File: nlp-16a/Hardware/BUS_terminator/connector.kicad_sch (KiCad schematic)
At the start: 37 parts, among them J1 Conn_02x20_Odd_Even, J2 Conn_02x20_Odd_Even, J3 Conn_02x20_Odd_Even, J4 Conn_02x10_Odd_Even, J5 Screw_Terminal_01x02, J6 Conn_02x16_Odd_Even, J7 Conn_02x16_Odd_Even

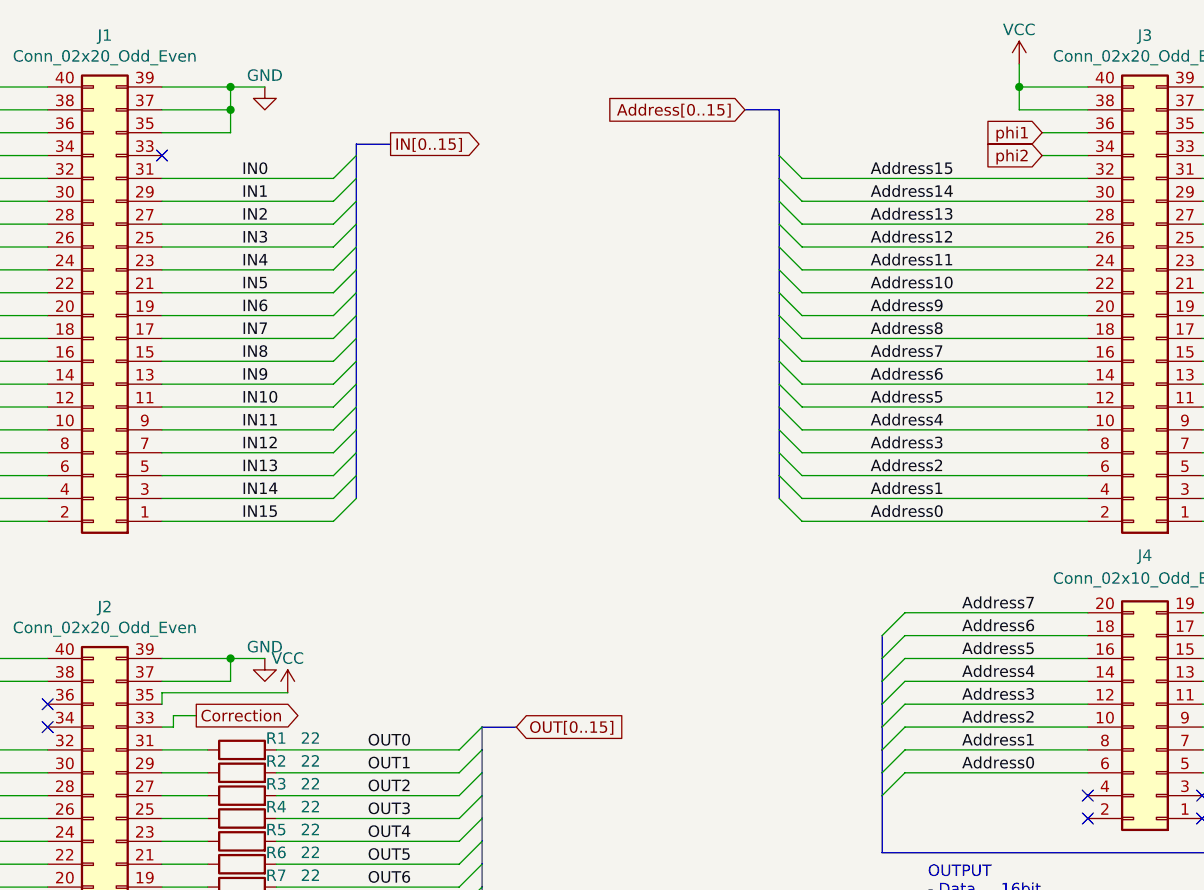
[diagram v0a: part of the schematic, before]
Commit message: バスターミネータのDMA機能は不要と判断したので削除．必要ならば外部回路で実現するように
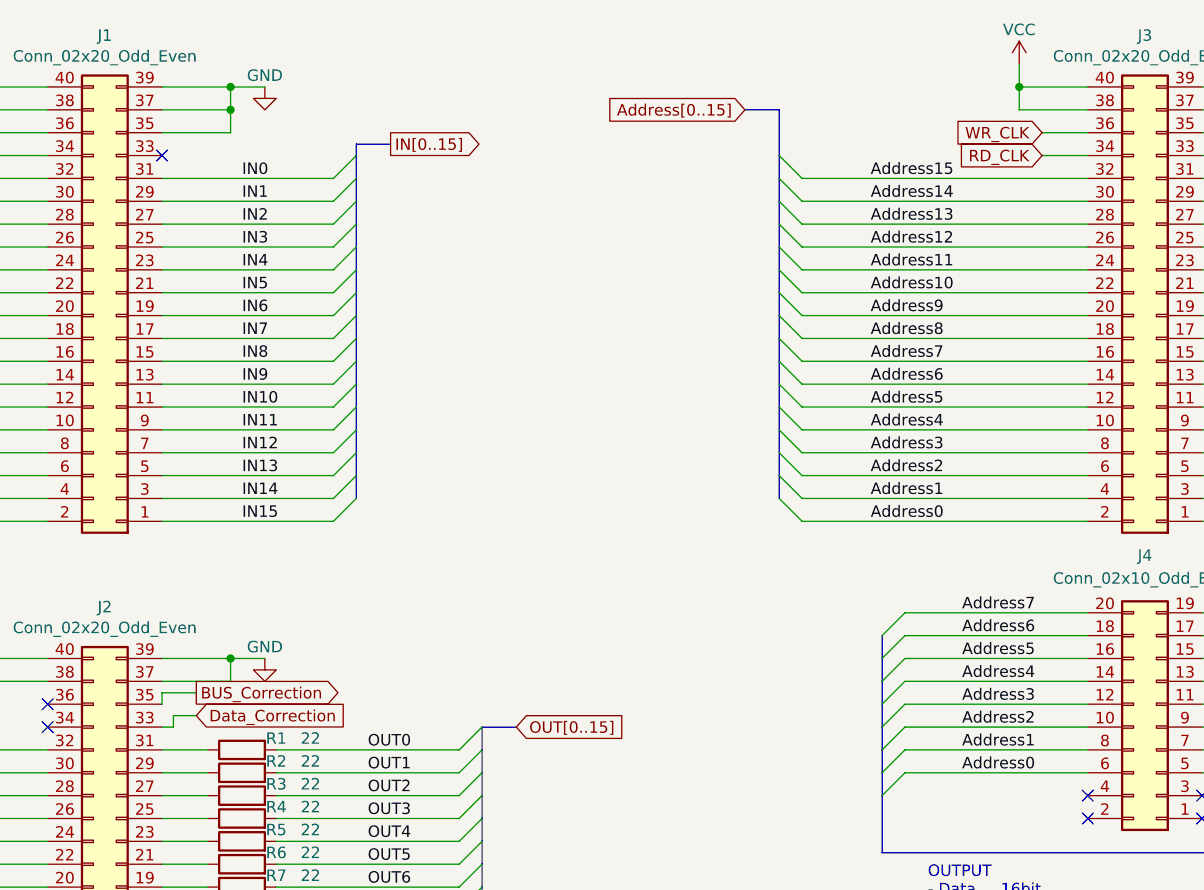
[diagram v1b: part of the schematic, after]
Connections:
- net VCC: no longer J2.35 (Pin_35)
- net phi1: no longer J3.36 (Pin_36)
- net phi2: no longer J3.34 (Pin_34)
- net Correction renamed Data_Correction
- new net BUS_Correction: J2.35 (Pin_35)
- new net RD_CLK: J3.34 (Pin_34)
- new net WR_CLK: J3.36 (Pin_36)
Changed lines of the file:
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@@
+    (stroke (width 0) (type default) (color 0 0 0 0))
+  )
+  (wire (pts (xy 101.6 87.63) (xy 105.41 87.63))
     (stroke (width 0) (type default) (color 0 0 0 0))
   )
@@
   )
   (wire (pts (xy 204.47 22.86) (xy 196.85 22.86))
-    (stroke (width 0) (type default) (color 0 0 0 0))
-  )
-  (wire (pts (xy 101.6 87.63) (xy 115.57 87.63))
     (stroke (width 0) (type default) (color 0 0 0 0))
   )
@@
     (effects (font (size 1.27 1.27)) (justify left bottom))
   )
-  (global_label "phi1" (shape input) (at 199.39 25.4 180) (fields_autoplaced)
+  (global_label "WR_CLK" (shape input) (at 199.39 25.4 180) (fields_autoplaced)
     (effects (font (size 1.27 1.27)) (justify right))
-    (property "Intersheet References" "${INTERSHEET_REFS}" (id 0) (at 192.8645 25.3206 0)
+    (property "Intersheet References" "${INTERSHEET_REFS}" (id 0) (at 189.7198 25.3206 0)
       (effects (font (size 1.27 1.27)) (justify right) hide)
     )
@@
     )
   )
-  (global_label "Correction" (shape output) (at 105.41 90.17 0) (fields_autoplaced)
+  (global_label "Data_Correction" (shape input) (at 105.41 90.17 0) (fields_autoplaced)
     (effects (font (size 1.27 1.27)) (justify left))
-    (property "Intersheet References" "${INTERSHEET_REFS}" (id 0) (at 117.6202 90.0906 0)
+    (property "Intersheet References" "${INTERSHEET_REFS}" (id 0) (at 122.8817 90.0906 0)
       (effects (font (size 1.27 1.27)) (justify left) hide)
     )
@@
     )
   )
+  (global_label "BUS_Correction" (shape output) (at 105.41 87.63 0) (fields_autoplaced)
+    (effects (font (size 1.27 1.27)) (justify left))
+    (property "Intersheet References" "${INTERSHEET_REFS}" (id 0) (at 122.3979 87.5506 0)
+      (effects (font (size 1.27 1.27)) (justify left) hide)
+    )
+  )
   (global_label "A_SEL" (shape output) (at 48.26 132.08 180) (fields_autoplaced)
     (effects (font (size 1.27 1.27)) (justify right))
@@
     )
   )
-  (global_label "phi2" (shape input) (at 199.39 27.94 180) (fields_autoplaced)
+  (global_label "RD_CLK" (shape input) (at 199.39 27.94 180) (fields_autoplaced)
     (effects (font (size 1.27 1.27)) (justify right))
-    (property "Intersheet References" "${INTERSHEET_REFS}" (id 0) (at 192.8645 27.8606 0)
+    (property "Intersheet References" "${INTERSHEET_REFS}" (id 0) (at 189.9012 27.8606 0)
       (effects (font (size 1.27 1.27)) (justify right) hide)
     )
@@
     (pin "2")
   )
-  (symbol (lib_id "power:VCC") (at 115.57 87.63 0) (mirror y) (unit 1)
-    (in_bom yes) (on_board yes)
-    (property "Reference" "#PWR08" (id 0) (at 115.57 91.44 0)
-      (effects (font (size 1.27 1.27)) hide)
-    )
-    (property "Value" "VCC" (id 1) (at 115.57 83.82 0))
-    (property "Footprint" "" (id 2) (at 115.57 87.63 0)
-      (effects (font (size 1.27 1.27)) hide)
-    )
-    (property "Datasheet" "" (id 3) (at 115.57 87.63 0)
-      (effects (font (size 1.27 1.27)) hide)
-    )
-    (pin "1")
-  )
   (symbol (lib_id "Device:C") (at 105.41 175.26 0) (unit 1)

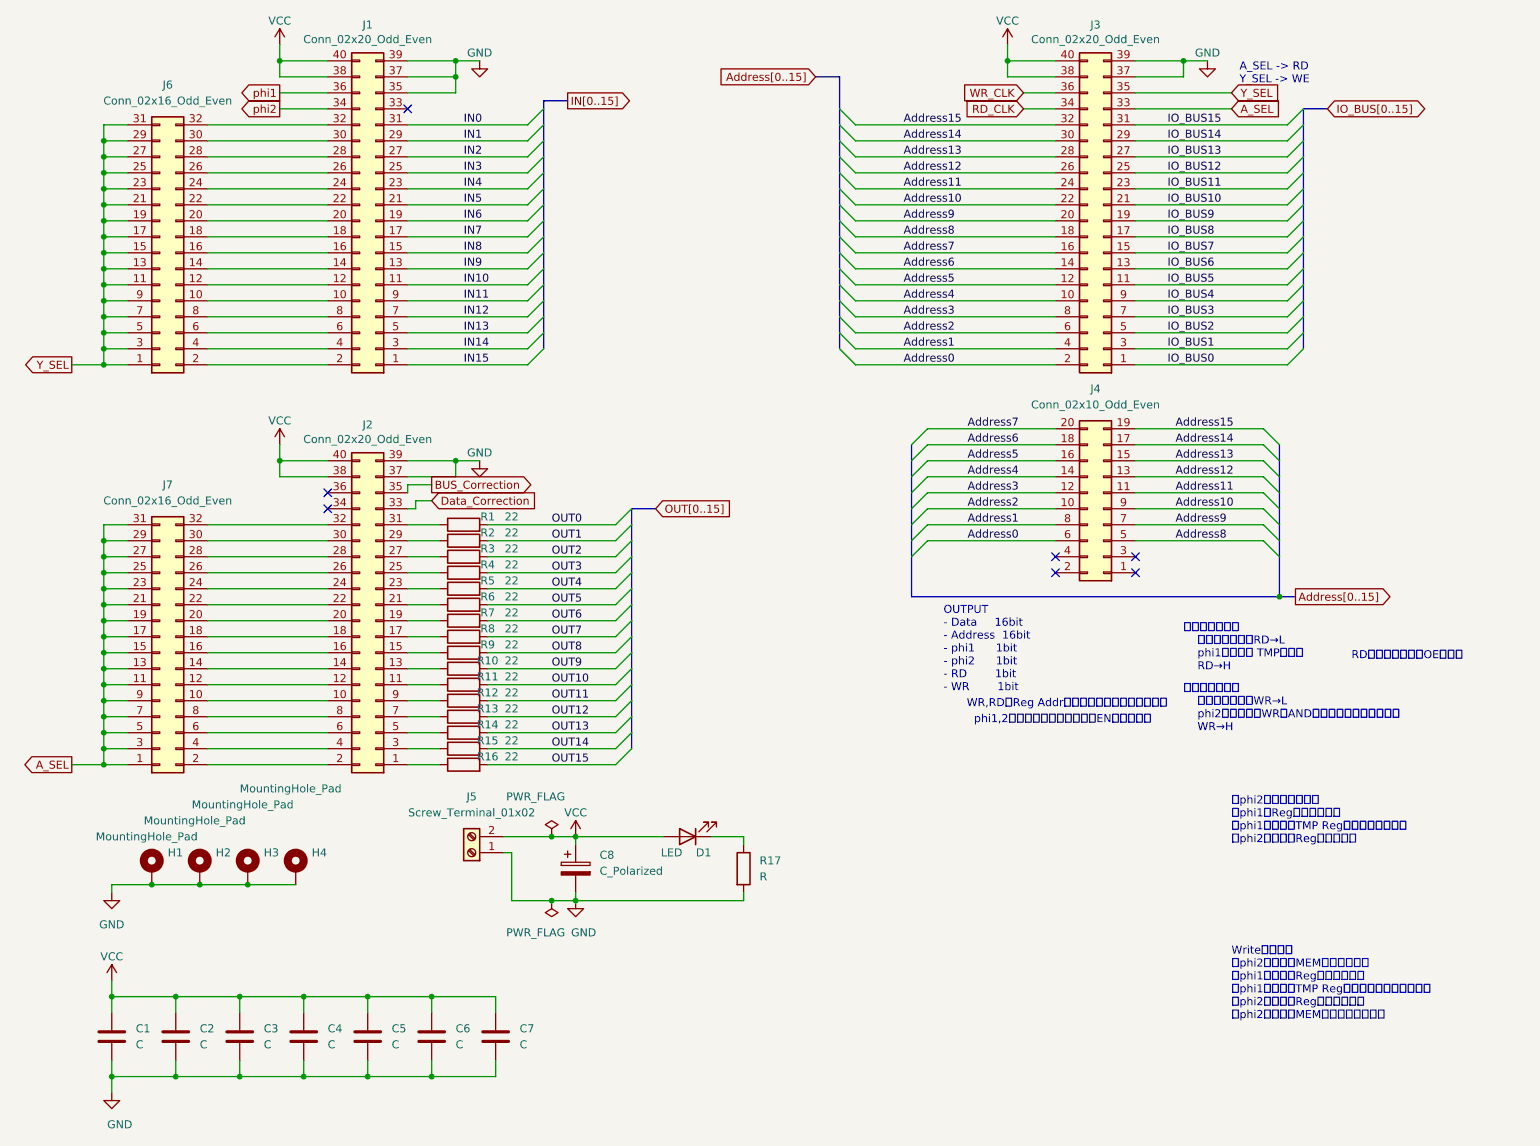
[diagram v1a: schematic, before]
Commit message: v1.1全ガーバーを更新
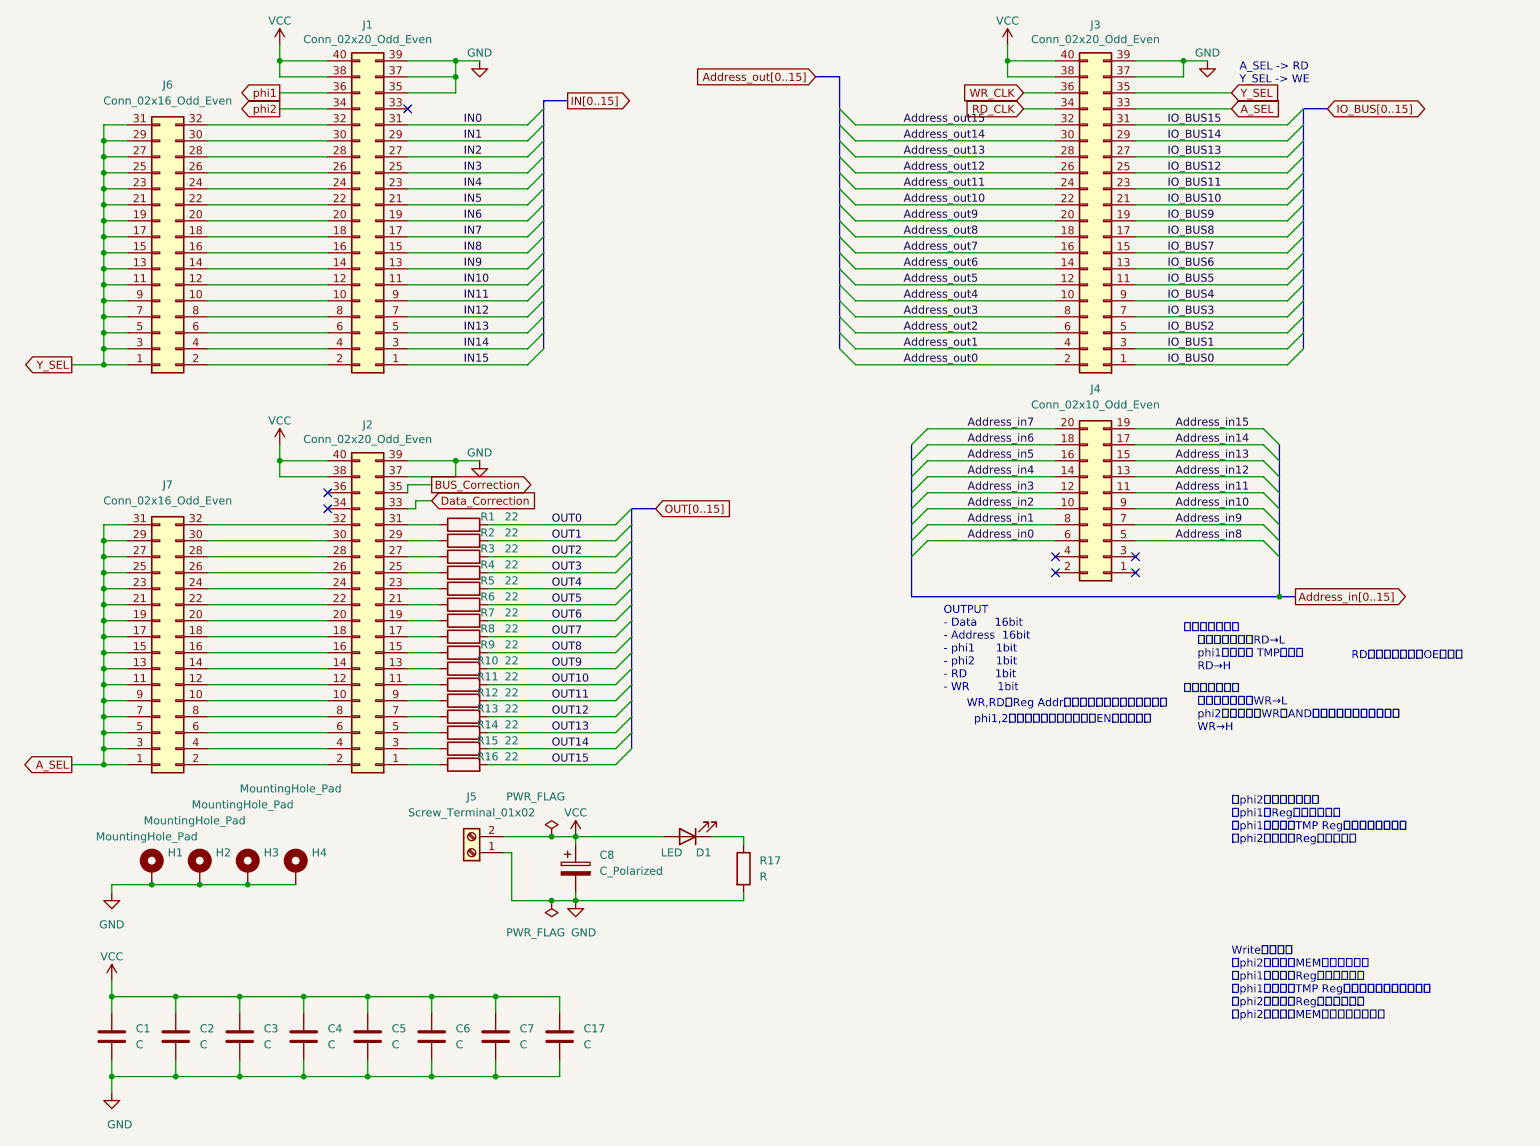
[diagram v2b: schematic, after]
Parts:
- added C17: C, Capacitor_THT:C_Disc_D7.0mm_W2.5mm_P5.00mm, symbol Device:C
- C1, C2, C3, C4, C5, C6, C7: footprint Capacitor_THT:C_Disc_D7.5mm_W2.5mm_P5.00mm -> Capacitor_THT:C_Disc_D7.0mm_W2.5mm_P5.00mm
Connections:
- net GND: now also C17.2
- net VCC: now also C17.1
- net Address0 renamed Address_in0
- net Address_in0: no longer J3.2 (Pin_2)
- net Address1 renamed Address_in1
- net Address_in1: no longer J3.4 (Pin_4)
- net Address10 renamed Address_in10
- net Address_in10: no longer J3.22 (Pin_22)
- net Address11 renamed Address_in11
- net Address_in11: no longer J3.24 (Pin_24)
- net Address12 renamed Address_in12
- net Address_in12: no longer J3.26 (Pin_26)
- net Address13 renamed Address_in13
- net Address_in13: no longer J3.28 (Pin_28)
- net Address14 renamed Address_in14
- net Address_in14: no longer J3.30 (Pin_30)
- net Address15 renamed Address_in15
- net Address_in15: no longer J3.32 (Pin_32)
- net Address2 renamed Address_in2
- net Address_in2: no longer J3.6 (Pin_6)
- net Address3 renamed Address_in3
- net Address_in3: no longer J3.8 (Pin_8)
- net Address4 renamed Address_in4
- net Address_in4: no longer J3.10 (Pin_10)
- net Address5 renamed Address_in5
- net Address_in5: no longer J3.12 (Pin_12)
- net Address6 renamed Address_in6
- net Address_in6: no longer J3.14 (Pin_14)
- net Address7 renamed Address_in7
- net Address_in7: no longer J3.16 (Pin_16)
- net Address8 renamed Address_in8
- net Address_in8: no longer J3.18 (Pin_18)
- net Address9 renamed Address_in9
- net Address_in9: no longer J3.20 (Pin_20)
- new net Address_out0: J3.2 (Pin_2)
- new net Address_out1: J3.4 (Pin_4)
- new net Address_out10: J3.22 (Pin_22)
- new net Address_out11: J3.24 (Pin_24)
- new net Address_out12: J3.26 (Pin_26)
- new net Address_out13: J3.28 (Pin_28)
- new net Address_out14: J3.30 (Pin_30)
- new net Address_out15: J3.32 (Pin_32)
- new net Address_out2: J3.6 (Pin_6)
- new net Address_out3: J3.8 (Pin_8)
- new net Address_out4: J3.10 (Pin_10)
- new net Address_out5: J3.12 (Pin_12)
- new net Address_out6: J3.14 (Pin_14)
- new net Address_out7: J3.16 (Pin_16)
- new net Address_out8: J3.18 (Pin_18)
- new net Address_out9: J3.20 (Pin_20)
